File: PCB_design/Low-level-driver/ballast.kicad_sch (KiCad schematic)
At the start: 34 parts, among them Q701 BC846BPN, Q702 BC846BPN, Q703 BC846BPN, Q704 BC846BPN, Q705 BC846BPN, Q706 BC846BPN, Q707 BC846BPN, Q708 BC846BPN, U701 TMUX1208PWR

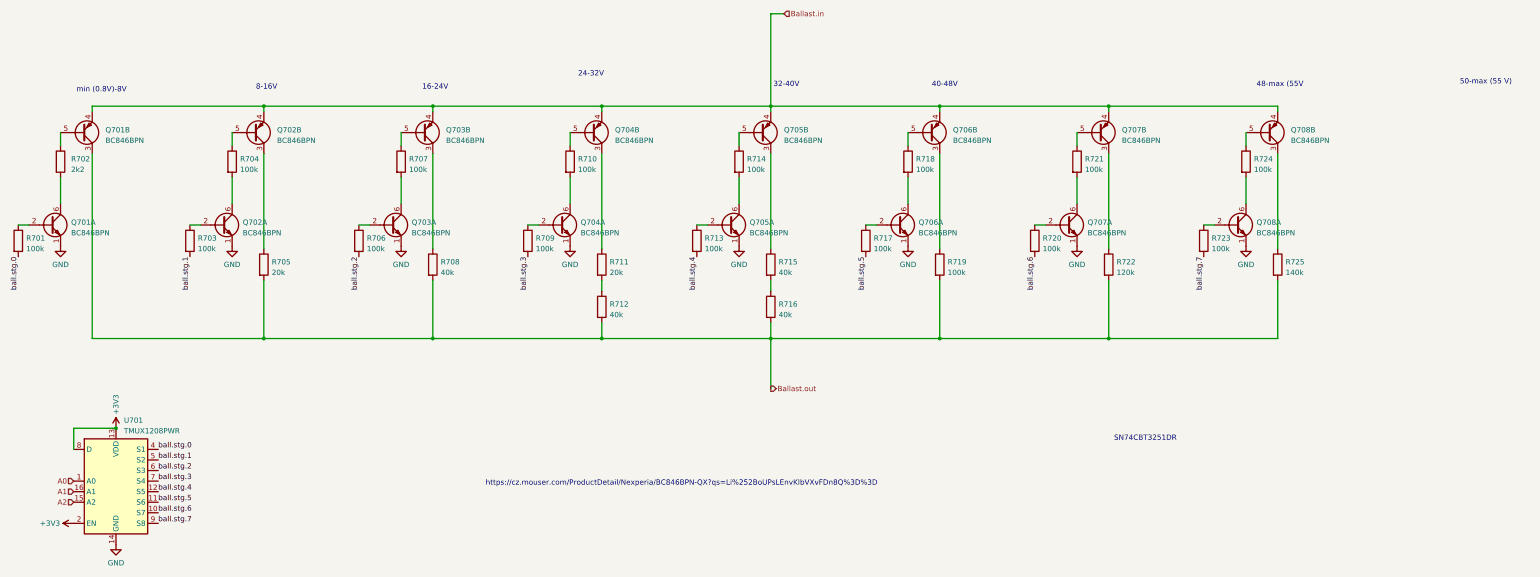
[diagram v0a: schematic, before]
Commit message: Schematic hierarchical redesign
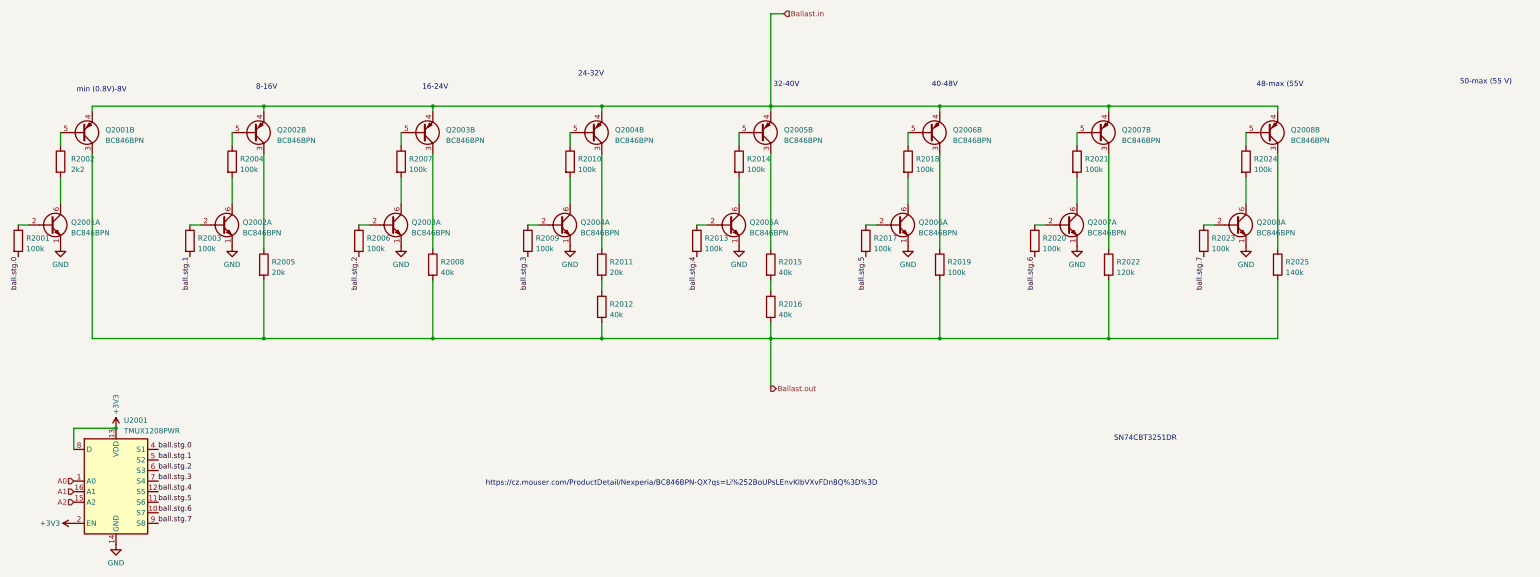
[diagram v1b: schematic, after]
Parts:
- renumbered Q701 to Q2001, Q702 to Q2002, Q703 to Q2003, Q704 to Q2004, Q705 to Q2005, Q706 to Q2006, Q707 to Q2007, Q708 to Q2008, R701 to R2001, R702 to R2002, R703 to R2003, R704 to R2004, R705 to R2005, R706 to R2006, R707 to R2007, R708 to R2008, R709 to R2009, R710 to R2010, R711 to R2011, R712 to R2012, R713 to R2013, R714 to R2014, R715 to R2015, R716 to R2016, R717 to R2017, R718 to R2018, R719 to R2019, R720 to R2020, R721 to R2021, R722 to R2022, R723 to R2023, R724 to R2024, R725 to R2025, U701 to U2001
